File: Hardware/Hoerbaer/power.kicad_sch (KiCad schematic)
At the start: 47 parts, among them J12 Barrel 2mm / 6mm, J13 Battery 2S Li-Ion, Q1 FDS6680A, Q2 SiS412DN, Q3 SiS412DN, Q4 FDS6680A, U8 TPS7A66, U9 bq24725A

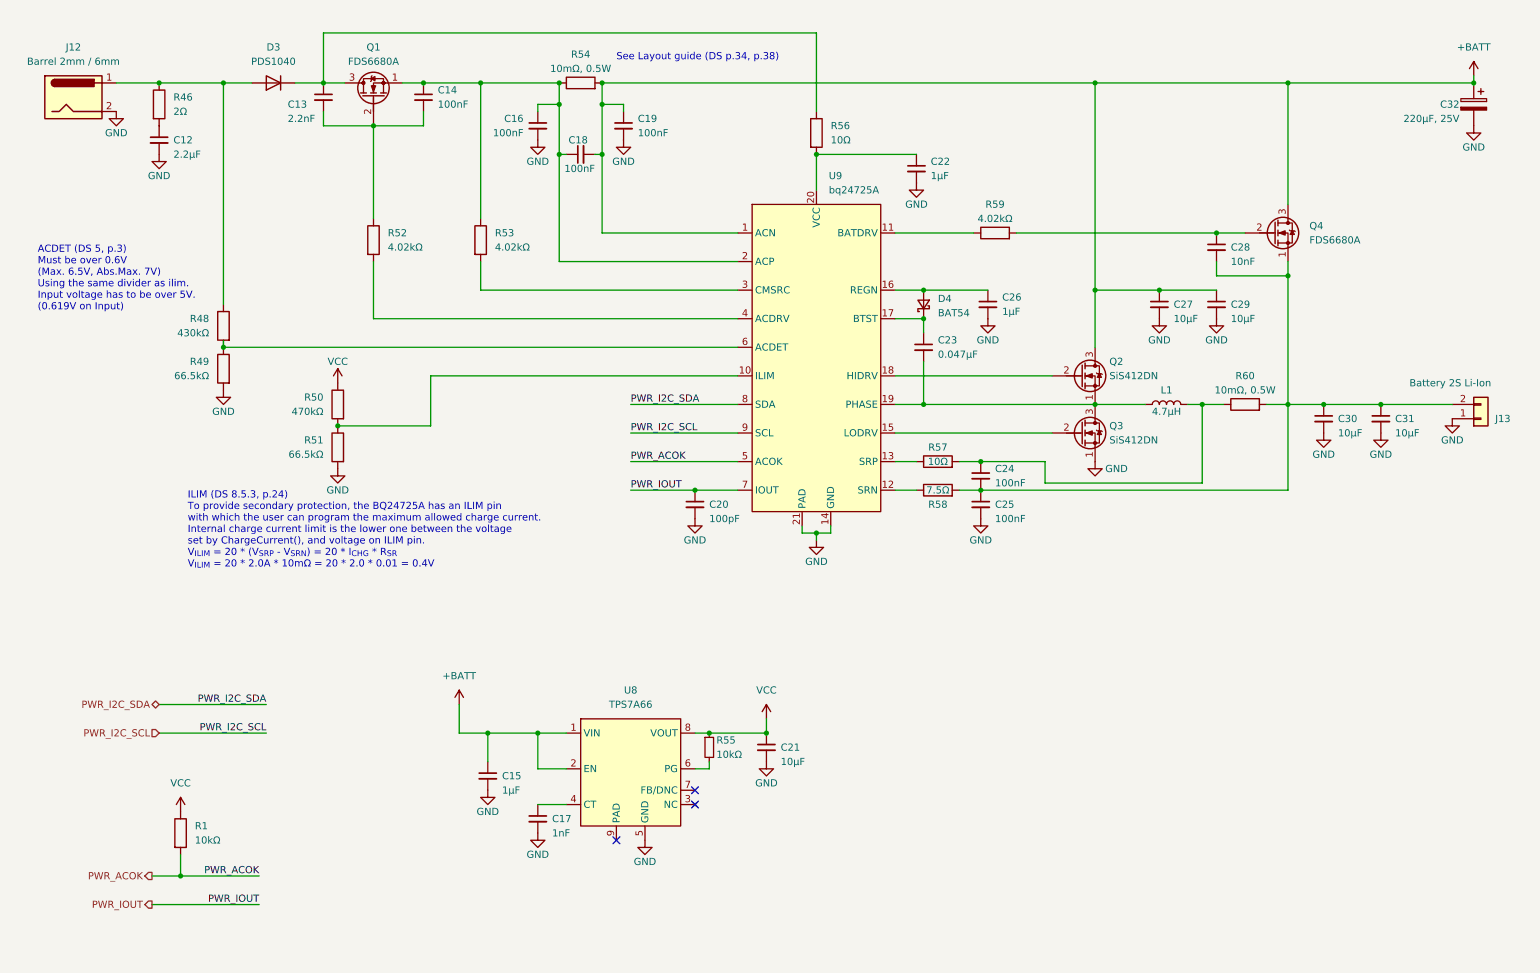
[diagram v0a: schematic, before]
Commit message: Nearly complete schematic with TLV61048 as 12V booster.
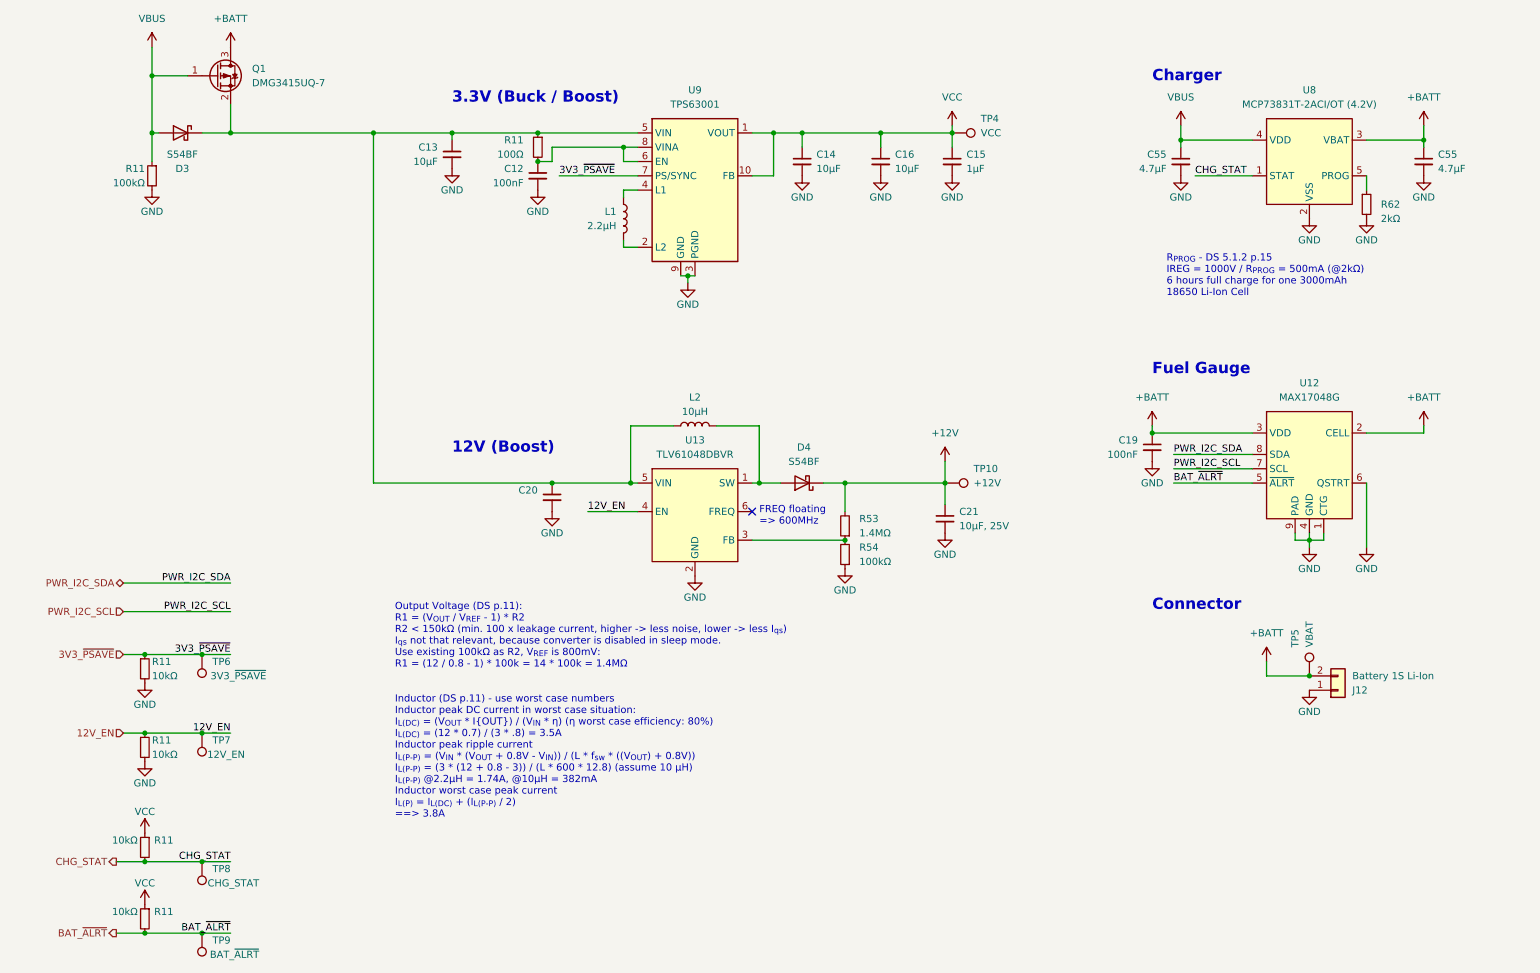
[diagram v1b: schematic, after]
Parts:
- removed C17: 1nF, symbol Device:C_Small
- removed C18, C24, C25: 100nF, symbol Device:C_Small
- removed C22, C26: 1µF, symbol Device:C_Small
- removed C23: 0.047µF, symbol Device:C_Small
- removed C27, C29, C30, C31: 10µF, symbol Device:C_Small
- removed C28: 10nF, symbol Device:C_Small
- removed C32: 220µF, 25V, symbol Device:C_Polarized
- removed D3: PDS1040, Diode_SMD:D_PowerDI-5, symbol Device:D
- removed D4: BAT54, Baer_Footprints:SOT-23-D-ANK, symbol Device:D_Schottky_Small
- removed J12: Barrel 2mm / 6mm, symbol Connector:Barrel_Jack
- removed J13: Battery 2S Li-Ion, Connector_Wire:SolderWire-0.75sqmm_1x02_P7mm_D1.25mm_OD3.5mm, symbol Connector_Generic:Conn_01x02
- removed Q1, Q4: FDS6680A, symbol Device:Q_NMOS_SGD
- removed Q2, Q3: SiS412DN, symbol Device:Q_NMOS_SGD
- removed R1: 10kΩ, symbol Device:R
- removed R46: 2Ω, symbol Device:R
- removed R48: 430kΩ, symbol Device:R
- removed R49, R51: 66.5kΩ, symbol Device:R
- removed R50: 470kΩ, symbol Device:R
- removed R52, R53, R59: 4.02kΩ, symbol Device:R
- removed R54, R60: 10mΩ, 0.5W, symbol Device:R
- removed R55: 10kΩ, symbol Device:R_Small
- removed R56, R57: 10Ω, symbol Device:R
- removed R58: 7.5Ω, symbol Device:R
- removed U8: TPS7A66, Package_SO:HVSSOP-8-1EP_3x3mm_P0.65mm_EP1.57x1.89mm_ThermalVias, symbol Baer_Symbols:TPS7A66-Q1
- removed U9: bq24725A, Package_DFN_QFN:QFN-20-1EP_3.5x3.5mm_P0.5mm_EP2x2mm_ThermalVias, symbol Baer_Symbols:bq24725A
- added C55 (x2): 4.7µF, symbol Device:C_Small
- added D3, D4: S54BF, Baer_Footprints:S54BF, symbol Device:D_Schottky
- added J12: Battery 1S Li-Ion, Connector_Wire:SolderWire-0.75sqmm_1x02_P7mm_D1.25mm_OD3.5mm, symbol Connector_Generic:Conn_01x02
- added L2: 10µH, Inductor_SMD:L_10.4x10.4_H4.8, symbol Device:L
- added Q1: DMG3415UQ-7, Package_TO_SOT_SMD:SOT-23, symbol Device:Q_PMOS_GSD
- added R11 (x4): 10kΩ, symbol Device:R_Small
- added R11, R54: 100kΩ, symbol Device:R_Small
- added R11: 100Ω, symbol Device:R_Small
- added R53: 1.4MΩ, Resistor_SMD:R_0603_1608Metric, symbol Device:R_Small
- added R62: 2kΩ, symbol Device:R_Small
- added TP10: +12V, TestPoint:TestPoint_Pad_D1.5mm, symbol Connector:TestPoint
- added TP4: VCC, TestPoint:TestPoint_Pad_D1.5mm, symbol Connector:TestPoint
- added TP5: VBAT, TestPoint:TestPoint_Pad_D1.5mm, symbol Connector:TestPoint
- added TP6: 3V3_~{PSAVE}, TestPoint:TestPoint_Pad_D1.5mm, symbol Connector:TestPoint
- added TP7: 12V_EN, TestPoint:TestPoint_Pad_D1.5mm, symbol Connector:TestPoint
- added TP8: CHG_STAT, TestPoint:TestPoint_Pad_D1.5mm, symbol Connector:TestPoint
- added TP9: BAT_~{ALRT}, TestPoint:TestPoint_Pad_D1.5mm, symbol Connector:TestPoint
- added U12: MAX17048G, Baer_Footprints:TDFN-8-1EP_MAXIM, symbol Baer_Symbols:MAX17048 DFN8
- added U13: TLV61048DBVR, Package_TO_SOT_SMD:SOT-23-6, symbol Baer_Symbols:TLV61048
- added U8: MCP73831T-2ACI/OT (4.2V), Package_TO_SOT_SMD:SOT-23-5, symbol Baer_Symbols:MCP73831/2_SOT
- added U9: TPS63001, Package_SON:Texas_DRC0010J_ThermalVias, symbol Regulator_Switching:TPS63001
- C12: value 2.2µF -> 100nF
- C13: value 2.2nF -> 10µF
- C14, C16: value 100nF -> 10µF
- C20: value 100pF -> ~
- C21: value 10µF -> 10µF, 25V; JLCPCB (none) -> C128855; MPN (none) -> CC1206KKX5R8BB106
- L1: value 4.7µH -> 2.2µH; JLCPCB (none) -> C341775; MPN (none) -> LQH3NPN2R2MJRL
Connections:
- net PWR_IOUT is gone; now on an unnamed net: C20.1
- net +BATT: now also C55.1, J12.2 (Pin_2), Q1.3 (D), TP5.1, U12.2 (CELL), U12.3 (VDD), U8.3 (VBAT); no longer C15.1
- net GND: now also C13.2, C14.2, C55.2, C55.2, J12.1 (Pin_1), R11.2, R11.2, R11.2, R54.1, R62.2, U12.1 (CTG), U12.4 (GND), U12.6 (QSTRT), U12.9 (PAD), U13.2 (GND), U8.2 (VSS), U9.11 (PGND), U9.3 (PGND), U9.9 (GND)
- net PWR_I2C_SCL: now also U12.7 (SCL)
- net PWR_I2C_SDA: now also U12.8 (SDA)
- net VCC: now also C14.1, C15.1, C16.1, R11.1, R11.1, TP4.1, U9.1 (VOUT), U9.10 (FB); no longer C21.1
- net at C12.1: now also R11.2, U9.6 (EN), U9.8 (VINA)
- net at C13.1: now also D3.1 (K), L2.1, Q1.2 (S), R11.1, U13.5 (VIN), U9.5 (VIN)
- net at L1.1: now also U9.4 (L1)
- net at L1.2: now also U9.2 (L2)
- new net: R53.1, R54.2, U13.3 (FB)
- new net: D4.2 (A), L2.2, U13.1 (SW)
- new net: R62.1, U8.5 (PROG)
- new net +12V: C21.1, D4.1 (K), R53.2, TP10.1
- new net 12V_EN: R11.1, TP7.1, U13.4 (EN)
- new net 3V3_~{PSAVE}: R11.1, TP6.1, U9.7 (PS/SYNC)
- new net BAT_~{ALRT}: R11.2, TP9.1, U12.5 (~{ALRT})
- new net CHG_STAT: R11.2, TP8.1, U8.1 (STAT)
- new net VBUS: C55.1, D3.2 (A), Q1.1 (G), R11.1, U8.4 (VDD)
- no-connect marks 3 -> 1
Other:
- note added: "12V (Boost)"
- note added: "3.3V (Buck / Boost)"
- note added: "Charger"
- note added: "Connector"
- note added: "FREQ floating => 600MHz"
- note added: "Fuel Gauge"
- note added: "Inductor (DS p.11) - use worst case numbers Inductor peak DC current in worst case situation: I_{L(DC)} = (V_{OUT} * I{OUT}) / (V_{IN} * η) (η worst case efficiency: 80%) I_{L(DC)} = (12 * 0.7) / (3 * .8) = 3.5A Inductor peak ripple current I_{L(P-P)} = (V_{IN} * (V_{OUT} + 0.8V - V_{IN})) / (L * f_{sw} * ((V_{OUT}) + 0.8V)) I_{L(P-P)} = (3 * (12 + 0.8 - 3)) / (L * 600 * 12.8) (assume 10 µH) I_{L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"
- note added: "Output Voltage (DS p.11): R1 = (V_{OUT} / V_{REF} - 1) * R2 R2 < 150kΩ (min. 100 x leakage current, higher -> less noise, lower -> less I_{qs}) I_{qs} not that relevant, because converter is disabled in sleep mode. Use existing 100kΩ as R2, V_{REF} is 800mV: R1 = (12 / 0.8 - 1) * 100k = 14 * 100k = 1.4MΩ"
- note added: "R_{PROG} - DS 5.1.2 p.15 IREG = 1000V / R_{PROG} = 500mA (@2kΩ) 6 hours full charge for one 3000mAh 18650 Li-Ion Cell"
- note removed: "ACDET (DS 5, p.3) Must be over 0.6V (Max. 6.5V, Abs.Max. 7V) Using the same divider as ilim. Input voltage has to be over 5V. (0.619V on Input)"
- note removed: "ILIM (DS 8.5.3, p.24) To provide secondary protection, the BQ24725A has an ILIM pin with which the user can program the maximum allowed charge current. Internal charge current limit is the lower one between the voltage set by ChargeCurrent(), and voltage on ILIM pin. V_{ILIM} = 20 * (V_{SRP} - V_{SRN}) = 20 * I_{CHG} * R_{SR} V_{ILIM} = 20 * 2.0A * 10mΩ = 20 * 2.0 * 0.01 = 0.4V"
- note removed: "See Layout guide (DS p.34, p.38)"
- company: (none) -> Drachosaurus Designs
- title: (none) -> Hör Bär main

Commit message: Footprints, order numbers, ...
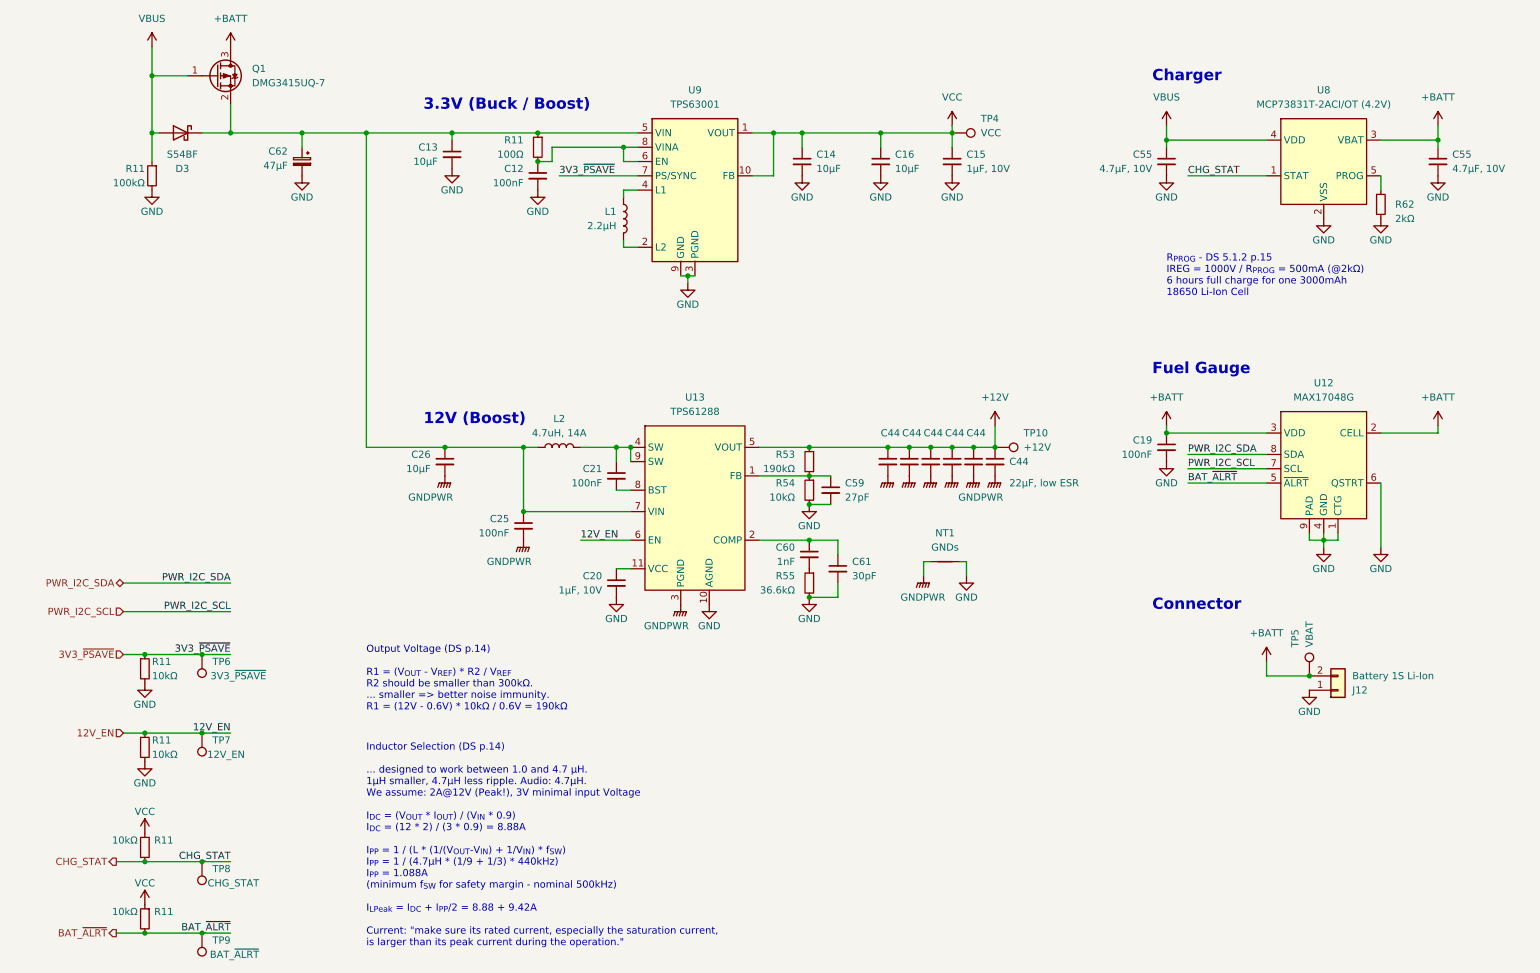
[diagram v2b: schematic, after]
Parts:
- removed D4: S54BF, Baer_Footprints:S54BF, symbol Device:D_Schottky
- removed U13: TLV61048DBVR, Package_TO_SOT_SMD:SOT-23-6, symbol Baer_Symbols:TLV61048
- added C25: 100nF, Capacitor_SMD:C_0402_1005Metric, symbol Device:C_Small
- added C26: 10µF, Capacitor_SMD:C_0805_2012Metric, symbol Device:C_Small
- added C44 (x6): 22µF, low ESR, Capacitor_SMD:C_1210_3225Metric, symbol Device:C_Small
- added C59: 27pF, Capacitor_SMD:C_0402_1005Metric, symbol Device:C_Small
- added C60: 1nF, Capacitor_SMD:C_0402_1005Metric, symbol Device:C_Small
- added C61: 30pF, Capacitor_SMD:C_0402_1005Metric, symbol Device:C_Small
- added C62: 47µF, Capacitor_SMD:CP_Elec_6.3x5.9, symbol Device:C_Polarized_Small
- added NT1: GNDs, NetTie:NetTie-2_THT_Pad0.3mm, symbol Device:NetTie_2
- added R55: 36.6kΩ, Resistor_SMD:R_0402_1005Metric, symbol Device:R_Small
- added U13: TPS61288, Package_DFN_QFN:Texas_VQFN-HR-20_3x2.5mm_P0.5mm_RQQ0011A, symbol Baer_Symbols:TPS61288
- C12, C19: footprint (none) -> Capacitor_SMD:C_0402_1005Metric
- C13, C14, C16: footprint (none) -> Capacitor_SMD:C_0805_2012Metric; JLCPCB (none) -> C6119932; MPN (none) -> CGA0805X7R106K250MT
- C15: value 1µF -> 1µF, 10V; footprint (none) -> Capacitor_SMD:C_0402_1005Metric; JLCPCB (none) -> C726581; MPN (none) -> AC0805KKX7R6BB105
- C20: value ~ -> 1µF, 10V; footprint (none) -> Capacitor_SMD:C_0402_1005Metric; JLCPCB (none) -> C726581; MPN (none) -> AC0805KKX7R6BB105
- C21: value 10µF, 25V -> 100nF; footprint (none) -> Capacitor_SMD:C_0402_1005Metric; JLCPCB C128855 -> (none); MPN CC1206KKX5R8BB106 -> (none)
- C55: value 4.7µF -> 4.7µF, 10V; footprint (none) -> Capacitor_SMD:C_0805_2012Metric; JLCPCB (none) -> C361188; MPN (none) -> C2012X7R1A475KT0J0E
- L1: footprint (none) -> Baer_Footprints:L_Murata_LQH3NPN
- L2: value 10µH -> 4.7uH, 14A; footprint Inductor_SMD:L_10.4x10.4_H4.8 -> Baer_Footprints:L_TDK_SPM12565; JLCPCB C171586 -> C2048059; MPN CDRH104RT125NP-100MC -> SPM12565VT-4R7M-D Copy
- R11, R62: footprint (none) -> Resistor_SMD:R_0402_1005Metric
- R53: value 1.4MΩ -> 190kΩ; footprint Resistor_SMD:R_0603_1608Metric -> Resistor_SMD:R_0402_1005Metric; JLCPCB C170468 -> (none); MPN WR06W1404FTL -> (none)
- R54: value 100kΩ -> 10kΩ; footprint (none) -> Resistor_SMD:R_0402_1005Metric
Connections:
- net +12V: now also R53.1, C44.1, C44.1, C44.1, C44.1, C44.1, C44.1, U13.5 (VOUT); no longer C21.1, R53.2
- net 12V_EN: now also U13.6 (EN)
- net GND: now also R54.2, C59.2, C61.2, C62.2, NT1.2, R55.2, U13.10 (AGND); no longer C21.2, R54.1
- net at C13.1, D3.1 (K), L2.1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: now also C25.1, C26.1, C62.1, U13.7 (VIN); no longer C20.1
- net at L2.2: now also C21.1, U13.4 (SW), U13.9 (SW)
- new net: C60.1, C61.1, U13.2 (COMP)
- new net: C59.1, R53.2, R54.1, U13.1 (FB)
- new net: C20.1, U13.11 (VCC)
- new net: C21.2, U13.8 (BST)
- new net: C60.2, R55.1
- new net GNDPWR: C25.2, C26.2, C44.2, C44.2, C44.2, C44.2, C44.2, C44.2, NT1.1, U13.3 (PGND)
- no-connect marks 1 -> 0
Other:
- note added: "Inductor Selection (DS p.14) ... designed to work between 1.0 and 4.7 µH. 1µH smaller, 4.7µH less ripple. Audio: 4.7µH. We assume: 2A@12V (Peak!), 3V minimal input Voltage I_{DC} = (V_{OUT} * I_{OUT}) / (V_{IN} * 0.9) I_{DC} = (12 * 2) / (3 * 0.9) = 8.88A I_{PP} = 1 / (L * (1/(V_{OUT}-V_{IN}) + 1/V_{IN}) * f_{SW}) I_{PP} = 1 / (4.7µH * (1/9 + 1/3) * 440kHz) I_{PP} = 1.088A (minimum f_{SW} for saf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"
- note added: "Output Voltage (DS p.14) R1 = (V_{OUT} - V_{REF}) * R2 / V_{REF} R2 should be smaller than 300kΩ. ... smaller => better noise immunity. R1 = (12V - 0.6V) * 10kΩ / 0.6V = 190kΩ"
- note removed: "FREQ floating => 600MHz"
- note removed: "Inductor (DS p.11) - use worst case numbers Inductor peak DC current in worst case situation: I_{L(DC)} = (V_{OUT} * I{OUT}) / (V_{IN} * η) (η worst case efficiency: 80%) I_{L(DC)} = (12 * 0.7) / (3 * .8) = 3.5A Inductor peak ripple current I_{L(P-P)} = (V_{IN} * (V_{OUT} + 0.8V - V_{IN})) / (L * f_{sw} * ((V_{OUT}) + 0.8V)) I_{L(P-P)} = (3 * (12 + 0.8 - 3)) / (L * 600 * 12.8) (assume 10 µH) I_{L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"
- note removed: "Output Voltage (DS p.11): R1 = (V_{OUT} / V_{REF} - 1) * R2 R2 < 150kΩ (min. 100 x leakage current, higher -> less noise, lower -> less I_{qs}) I_{qs} not that relevant, because converter is disabled in sleep mode. Use existing 100kΩ as R2, V_{REF} is 800mV: R1 = (12 / 0.8 - 1) * 100k = 14 * 100k = 1.4MΩ"
- moved on the sheet: C19, C55, R62, TP10, U12, U8
